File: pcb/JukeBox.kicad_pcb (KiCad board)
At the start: 2 copper layers, 92 x 90 mm, 104 parts, among them J1 USB_C_Receptacle_USB2.0_16P, Q1 Q_NPN_BEC, SW1 SW_SPST, SW10 SW_SPST, SW11 SW_SPST, SW12 SW_SPST, SW2 SW_SPST, SW3 SW_SPST, SW4 SW_SPST, SW5 SW_SPST, SW6 SW_SPST, SW7 SW_SPST, SW8 SW_SPST, SW9 SW_SPST, U1 NCP1117-3.3_SOT223, U2 W25Q128JVS, U3 RP2040, U4 st7789v, U5 CAT24C512, Y2 ABM8-272-T3

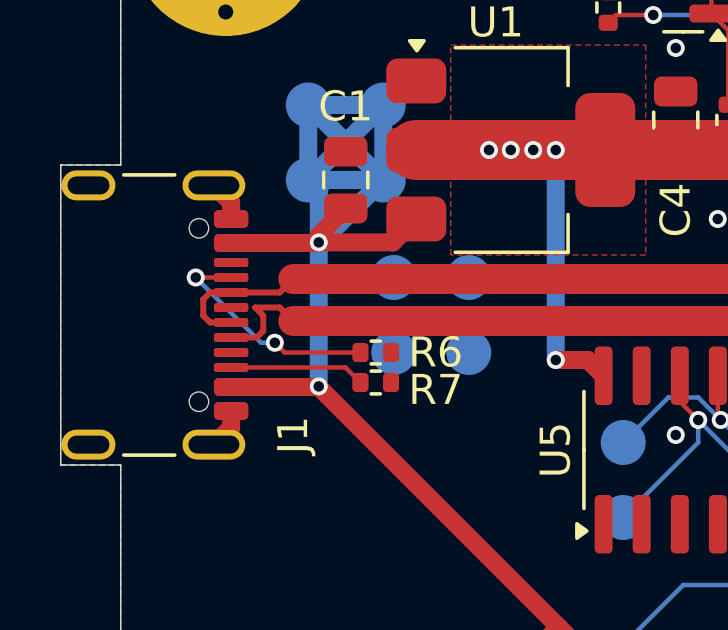
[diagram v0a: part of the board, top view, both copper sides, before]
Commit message: fix usb lines on pcb
oops.
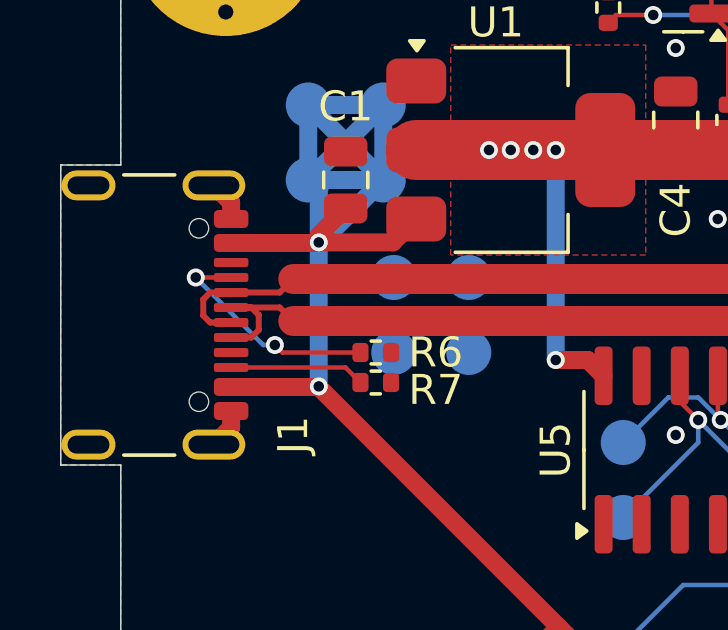
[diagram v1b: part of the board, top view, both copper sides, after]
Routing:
- net /USB_D+: track 73.8 -> 75.1 mm

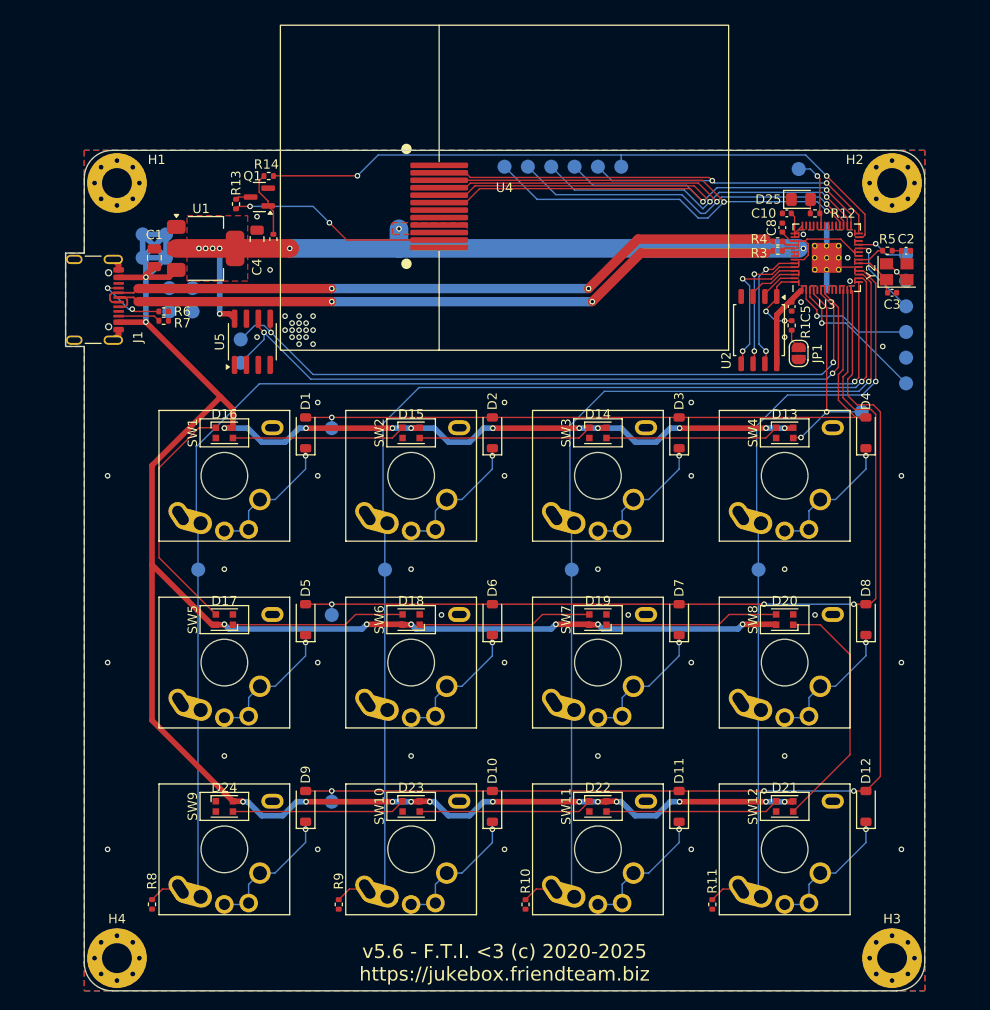
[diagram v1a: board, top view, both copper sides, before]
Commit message: massive pcb rework for rp2350
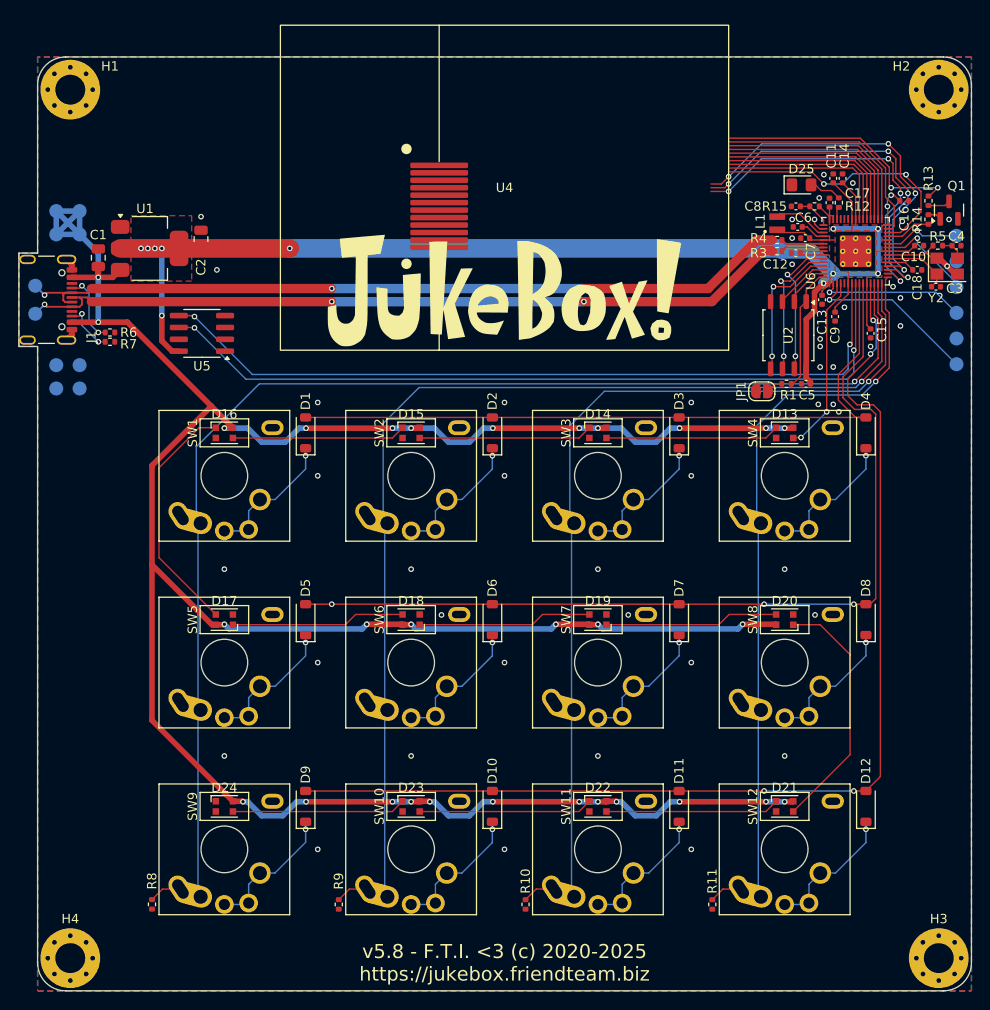
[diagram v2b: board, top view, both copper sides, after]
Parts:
- removed the TP21 at (94.1, 106.8)
- removed the TP22 at (94.1, 126.8)
- removed the TP23 at (94.1, 146.8)
- removed the TP24 at (79.8, 121.9)
- removed the TP25 at (99.8, 121.9)
- removed the TP26 at (119.8, 121.9)
- removed TP27, TP31, TP32, TP41, TP42, TP51, TP52, TP53, TP54, TP55, TP56: TestPoint, TestPoint:TestPoint_Pad_D1.5mm
- removed U3: RP2040, JukeBox:RP2040-QFN-56
- added C11: 100n, Capacitor_SMD:C_0402_1005Metric, F.Cu at (147.8, 80.0)
- added C12: 100n, Capacitor_SMD:C_0402_1005Metric, F.Cu at (143.8, 88.0)
- added C13: 100n, Capacitor_SMD:C_0402_1005Metric, F.Cu at (146.6, 93.0)
- added C14: 100n, Capacitor_SMD:C_0402_1005Metric, F.Cu at (148.8, 80.0)
- added C15: 100n, Capacitor_SMD:C_0402_1005Metric, F.Cu at (151.8, 96.6)
- added C16: 100n, Capacitor_SMD:C_0402_1005Metric, F.Cu at (155.4, 82.4)
- added C17: 100n, Capacitor_SMD:C_0402_1005Metric, F.Cu at (147.4, 82.6)
- added C18: 100n, Capacitor_SMD:C_0402_1005Metric, F.Cu at (156.8, 89.8)
- added C6: 4.7u, Capacitor_SMD:C_0402_1005Metric, F.Cu at (144.0, 85.2)
- added C7: 4.7u, Capacitor_SMD:C_0402_1005Metric, F.Cu at (144.8, 86.4)
- added C9: 100n, Capacitor_SMD:C_0402_1005Metric, F.Cu at (148.0, 94.8)
- added G1: LOGO, JukeBox:JukeBox, B.Cu at (112.6, 92.0)
- added L1: 3.3u, JukeBox:L_pol_2016, F.Cu at (141.8, 84.8)
- added TP10: TestPoint, TestPoint:TestPoint_Pad_D1.5mm, B.Cu at (62.3, 94.5)
- added TP11: TestPoint, TestPoint:TestPoint_Pad_D1.5mm, B.Cu at (62.3, 91.5)
- added U6: RP2350_60QFN, JukeBox:RP2350-QFN-60-1EP_7x7_P0.4mm_EP3.4x3.4mm_ThermalVias, F.Cu at (150.2, 87.8)
- C10, C8: value 1u -> 4.7u
- G1: moved to F.Cu
- R15: value 10k -> 33
- moved R13 74.2 mm to (158.0, 82.4), turned to 90 degrees
- moved Q1 73.9 mm to (160.2, 83.4), turned to 90 degrees
- moved R14 70.8 mm to (158.0, 84.4), turned to 90 degrees
- moved R15 58.1 mm to (145.8, 83.0), turned to 180 degrees
- moved TP16 14.6 mm to (67.1, 100.0)
- moved TP17 14.6 mm to (64.6, 100.0)
- moved TP18 14.6 mm to (67.1, 102.5)
- moved TP19 14.6 mm to (64.6, 102.5)
- moved C10 14.6 mm to (157.0, 87.2)
- moved H1 11.2 mm to (66.1, 70.5)
- moved H2 11.2 mm to (159.1, 70.5)
- moved TP12 9.58 mm to (67.1, 83.5)
- moved TP13 9.58 mm to (67.1, 86.0)
- moved TP14 9.58 mm to (64.6, 86.0)
- moved TP15 9.58 mm to (64.6, 83.5)
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- renumbered C4 to C2, C2 to C4, TP1 to TP12, TP2 to TP13, TP3 to TP14, TP4 to TP15, TP5 to TP16, TP6 to TP17, TP7 to TP18, TP8 to TP19, TP11 to TP21, TP12 to TP22, TP13 to TP23, TP14 to TP24, TP15 to TP25, TP16 to TP26
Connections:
- net /GPIO10 renamed /KBROW2
- net /GPIO11 renamed /KBROW3
- net /GPIO12 renamed /KBCOL1
- net /GPIO13 renamed /KBCOL2
- net /GPIO14 renamed /KBCOL3
- net /GPIO15 renamed /KBCOL4
- net /GPIO9 renamed /KBROW1
- C10 pad 1: GND -> +1V1
- C10 pad 2: +3V3 -> GND
- C8 pad 1: +1V1 -> /VREG_AVDD
- D13 pad 3: /GPIO2 -> /RGBDIN
- R12 pad 1: /GPIO25 -> /LEDPIN
- R14 pad 1: /GPIO16 -> /SCRBL
- R15 pad 2: Net-(Q1-B) -> /VREG_AVDD
- U4 pad 10: /GPIO21 -> /SCRDIN
- U4 pad 11: /GPIO17 -> /SCRRST
- U4 pad 7: /GPIO18 -> /SCRDC
- U4 pad 8: /GPIO19 -> /SCRCS
- U4 pad 9: /GPIO20 -> /SCRCLK
- U5 pad 5: /GPIO4 -> /I2C0SDA
- U5 pad 6: /GPIO5 -> /I2C0SCL
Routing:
- net /I2C0SCL: track 0.00 -> 84.5 mm, vias 0 -> 2
- net /I2C0SDA: track 0.00 -> 83.9 mm, vias 0 -> 2
- net /GPIO5: track 79.0 -> 0.00 mm, vias 2 -> 0
- net /GPIO4: track 76.7 -> 0.00 mm, vias 2 -> 0
- net /GPIO21: track 71.7 -> 0.00 mm, vias 2 -> 0
- net /GPIO16: track 71.1 -> 0.00 mm, vias 2 -> 0
- net /GPIO20: track 68.9 -> 0.00 mm, vias 2 -> 0
- net /GPIO19: track 66.4 -> 0.00 mm, vias 2 -> 0
- net /GPIO18: track 63.6 -> 0.00 mm, vias 2 -> 0
- net /GPIO17: track 61.6 -> 0.00 mm, vias 2 -> 0
- net +3V3: track 95.3 -> 152.3 mm, vias 12 -> 13
- net /SCRCS: track 0.00 -> 39.4 mm, vias 0 -> 4
- net /SCRDC: track 0.00 -> 38.9 mm, vias 0 -> 4
- net /SCRRST: track 0.00 -> 37.1 mm, vias 0 -> 4
- net /SCRCLK: track 0.00 -> 29.2 mm, vias 0 -> 2
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- added copper zone on F.Cu, net +1V1
- removed copper zone on B.Cu, net +3V3
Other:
- board size 92 x 90 mm -> 102 x 100 mm
- board text added: "v5.8 - F.T.I. <3 (c) 2020-2025 https://jukebox.friendteam.biz"
- board text removed: "v5.6 - F.T.I. <3 (c) 2020-2025 https://jukebox.friendteam.biz"

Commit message: add new screen footprint and route traces. update bom
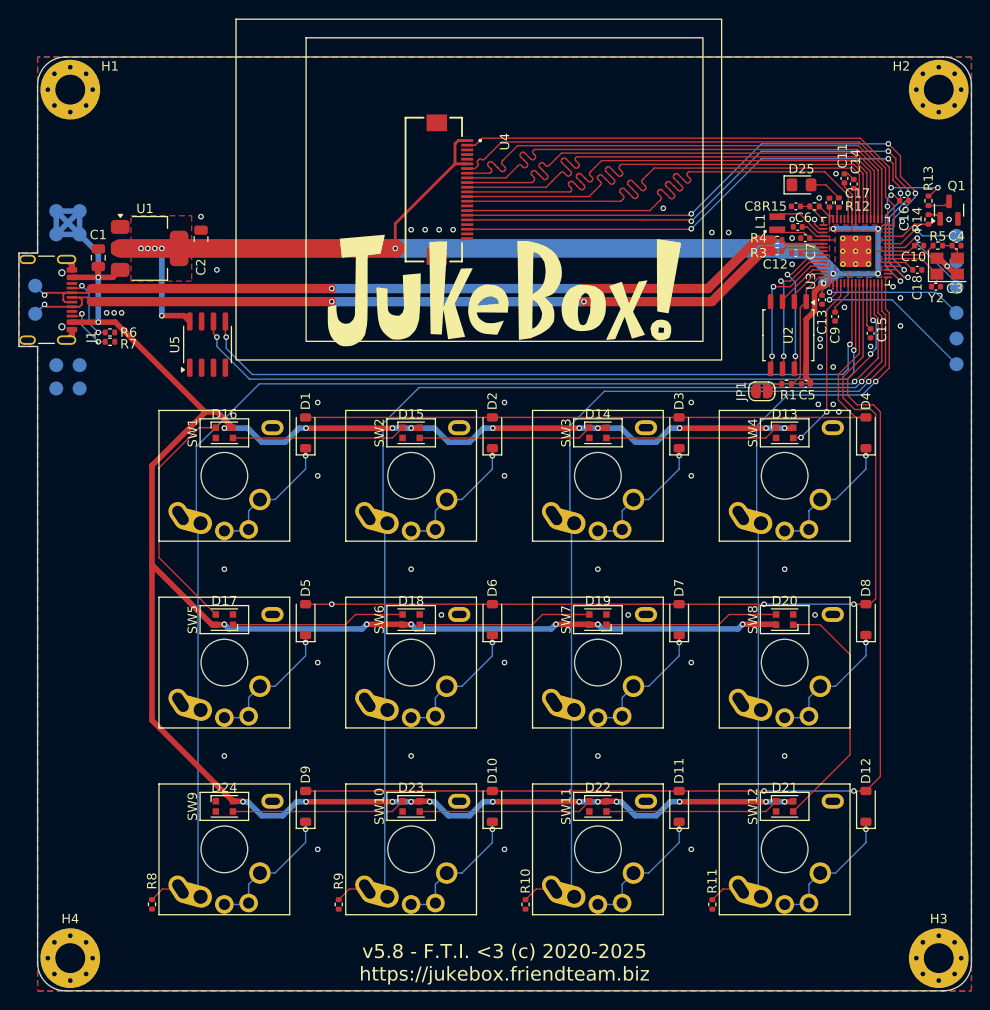
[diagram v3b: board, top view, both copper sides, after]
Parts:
- U4: value st7789v -> ~; footprint JukeBox:st7789v -> JukeBox:TFTQ-T20ST22ZP01
- moved U4 2.76 mm to (109.8, 81.2), turned to 0 degrees
- moved C14 1.34 mm to (150.0, 80.6)
- moved U5 1.34 mm to (80.8, 97.8), turned to 90 degrees
- moved C11 1.20 mm to (149.0, 80.0)
- renumbered U6 to U3
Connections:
- U3 pad 28: /SCRCLK -> /GPIO17
- U3 pad 40: /GPIO26_ADC0 -> /SCRCLK
- U4 pad 1: GND -> +3V3
- U4 pad 10: /SCRDIN -> /SCRD4
- U4 pad 11: /SCRRST -> /SCRD3
- U4 pad 12: GND -> /SCRD2
- U4 pad 3: +3V3 -> unconnected-(U4-NC-Pad3)
- U4 pad 4: +3V3 -> unconnected-(U4-NC-Pad4)
- U4 pad 5: GND -> unconnected-(U4-NC-Pad5)
- U4 pad 6: GND -> +3V3
- U4 pad 7: /SCRDC -> /SCRD7
- U4 pad 8: /SCRCS -> /SCRD6
- U4 pad 9: /SCRCLK -> /SCRD5
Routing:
- net /SCRD0: track 19.1 -> 54.9 mm
- net /SCRD1: track 19.7 -> 54.9 mm
- net /SCRD2: track 20.3 -> 54.9 mm
- net /SCRD3: track 20.9 -> 54.9 mm
- net /SCRD4: track 21.5 -> 54.9 mm
- net /SCRD5: track 22.2 -> 54.9 mm
- net /SCRD6: track 22.8 -> 54.9 mm
- net /SCRD7: track 25.4 -> 55.0 mm
- net /LEDK: track 27.1 -> 55.4 mm
- net /SCRRST: track 37.1 -> 64.9 mm
- net /SCRCS: track 39.4 -> 67.0 mm
- net /SCRDC: track 38.9 -> 66.4 mm
- net /SCRCLK: track 29.2 -> 54.9 mm, vias 2 -> 0
- net +3V3: track 152.3 -> 166.1 mm
- net /I2C0SDA: track 83.9 -> 80.3 mm
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
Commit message: more pcb updates
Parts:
- moved U4 2.50 mm to (109.8, 83.7)
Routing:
- net /SCRCLK: track 54.9 -> 20.7 mm
- net /SCRD0: track 54.9 -> 27.0 mm
- net /SCRDC: track 66.4 -> 42.3 mm
- net /SCRCS: track 67.0 -> 43.0 mm
- net /SCRRST: track 64.9 -> 40.9 mm
- net /SCRD1: track 54.9 -> 31.2 mm
- net /SCRD2: track 54.9 -> 33.9 mm
- net /SCRD3: track 54.9 -> 37.2 mm
- net +3V3: track 166.1 -> 149.5 mm
- net /SCRD4: track 54.9 -> 39.4 mm
- net /SCRD5: track 54.9 -> 43.0 mm
- net /SCRD6: track 54.9 -> 45.4 mm
- net /SCRD7: track 55.0 -> 49.7 mm
- net /LEDK: track 55.4 -> 53.5 mm

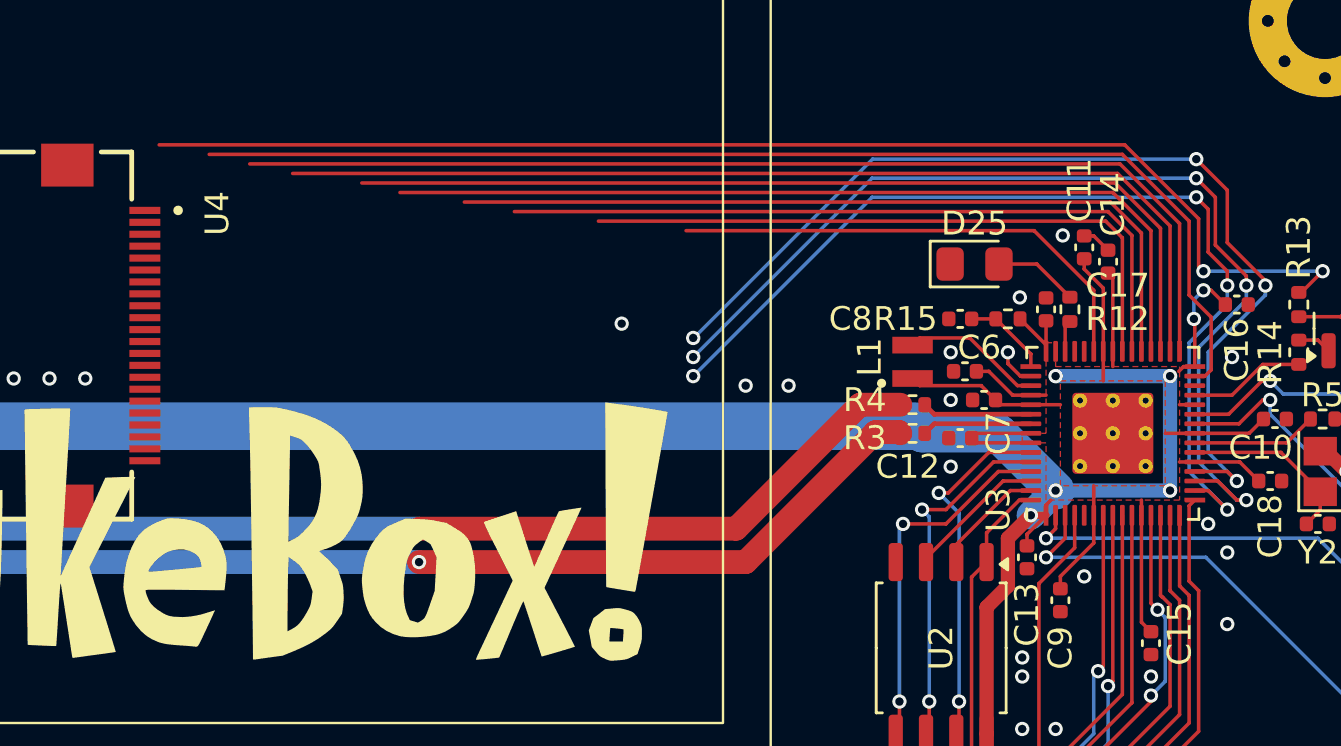
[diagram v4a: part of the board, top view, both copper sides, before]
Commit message: finalize screen placement on pcb, add spacer to scad, add bumps to legs for binding to the case better
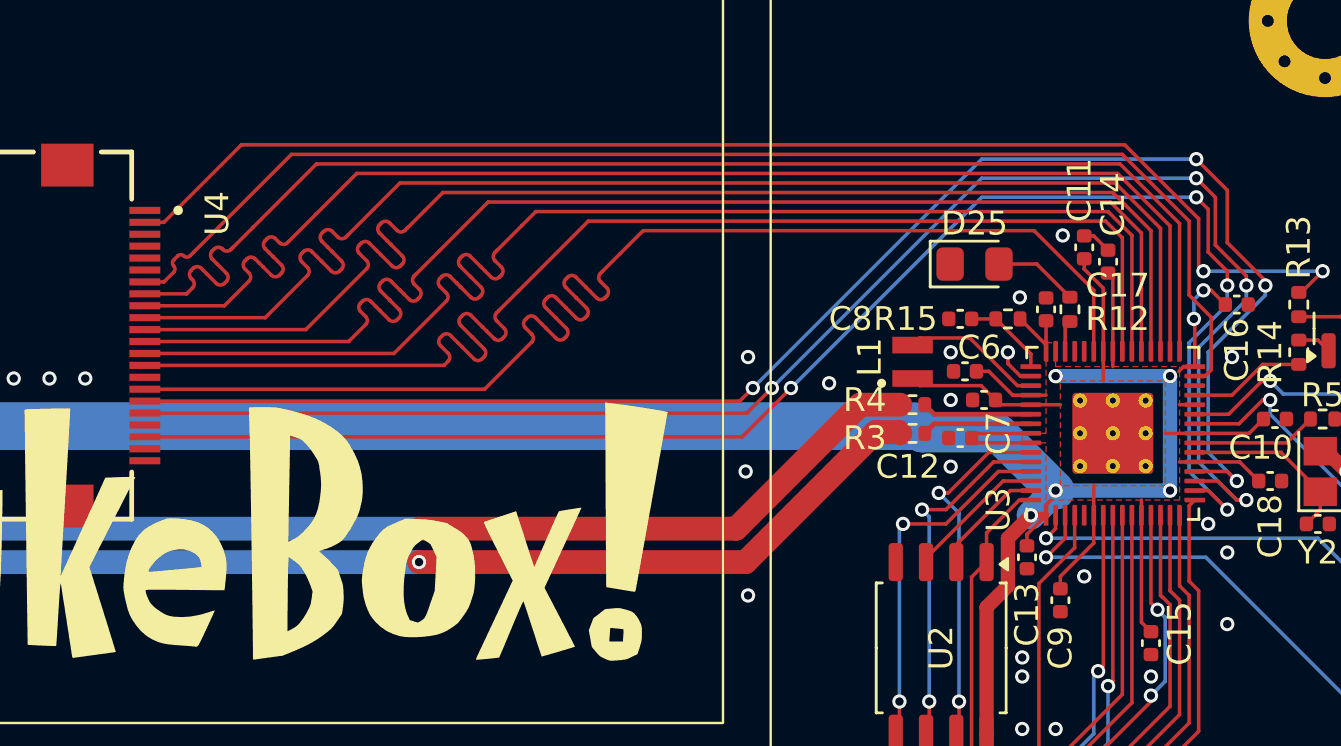
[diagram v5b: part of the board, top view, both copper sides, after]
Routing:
- net /SCRCLK: track 20.7 -> 54.9 mm
- net /SCRD0: track 27.0 -> 54.9 mm
- net /SCRDC: track 42.3 -> 66.4 mm
- net /SCRRST: track 40.9 -> 64.9 mm
- net /SCRCS: track 43.0 -> 66.9 mm
- net /SCRD1: track 31.2 -> 54.9 mm
- net /SCRD2: track 33.9 -> 54.9 mm
- net /SCRD3: track 37.2 -> 54.9 mm
- net /SCRD4: track 39.4 -> 54.9 mm
- net /SCRD5: track 43.0 -> 54.9 mm
- net /SCRD6: track 45.4 -> 54.9 mm
- net /SCRD7: track 49.7 -> 55.0 mm
- net /LEDK: track 53.5 -> 55.5 mm
- net GND: vias 56 -> 57
